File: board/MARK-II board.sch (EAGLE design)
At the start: 168 parts, among them IC1 MAX3243CPWR, IC10 IFX1963TBV, IC11 IFX1963TBV, IC12 ATMEGA48PB-AU, IC13 LD1117S33, IC2 FT230XS, IC3 ENC28J60SS, IC4 PCM5100, IC5 IS42S83200, IC6 MCP7940NSN, IC7 FM24CL16BG, IC8 AT25DN256SS, IC9 10M25SAE144, Q1 25MHz, Q2 32.768kHz, Q3 CMI-1275C-050, Q4 25MHz, Q5 18,432MHz, Q6 22.5792MHz, T1 BC337-16 A1, X1 MINI-USBUX60A-MB-5ST, X10 T821-106A1S100, X11 T821-110A1S100, X12 PJ-002BH-SMT-TR, X13 T821-106A1S100, X2 L717SDE09P1ACH4F, X3 L77HDE15SD1CH4R, X4 MD-60SM, X5 RB1-125BAG1A, X6 SJ1-3535NG, X7 MICROSD-HRS_DM3D, X8 BAT-HLD-002-SMT, X9 T821-120A1S100

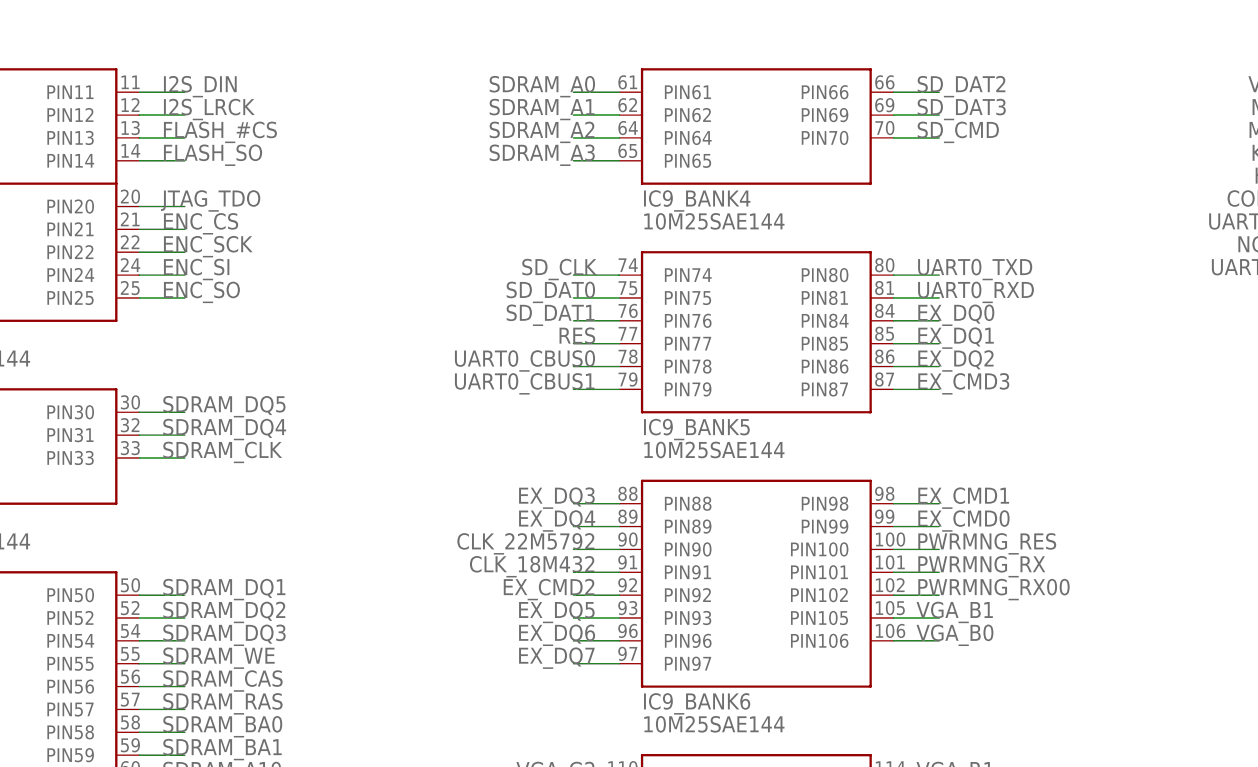
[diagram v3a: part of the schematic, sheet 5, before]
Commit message: Fixed pwrmng uart connection
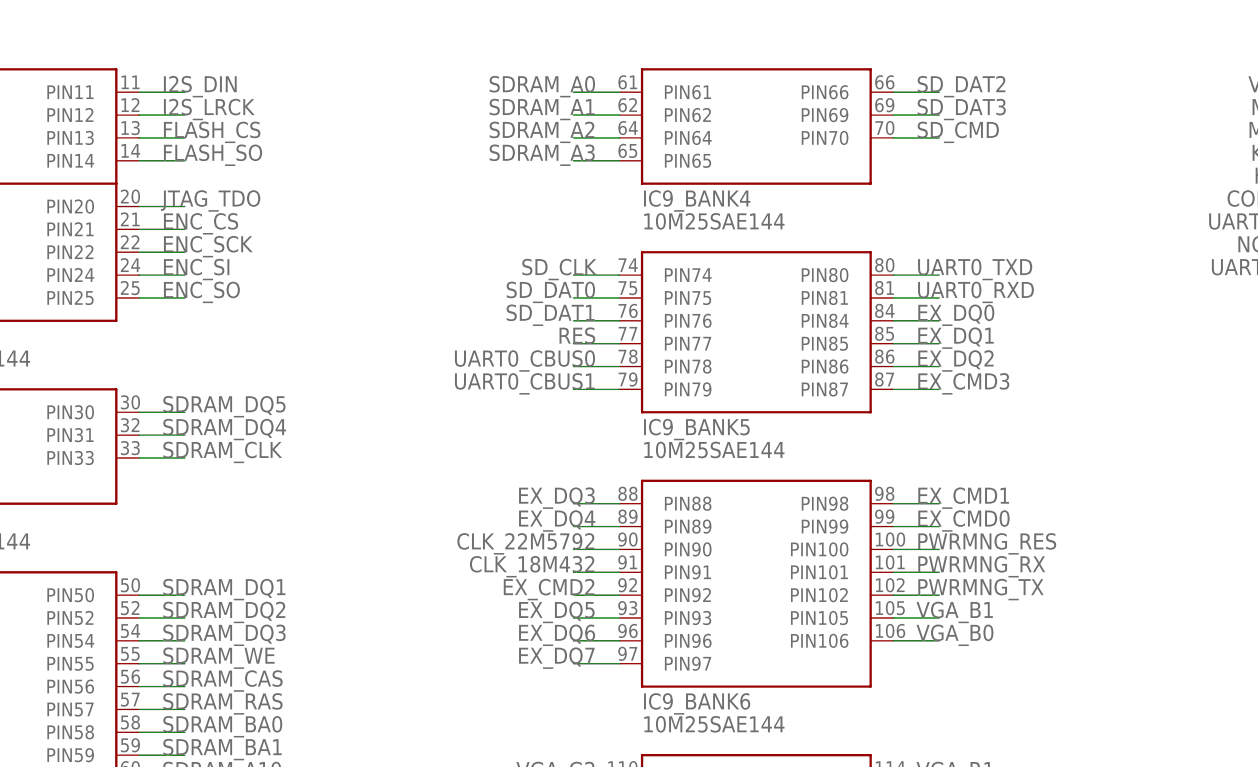
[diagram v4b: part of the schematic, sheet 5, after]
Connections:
- net FLASH_#CS renamed FLASH_CS
- removed net PWRMNG_RX00: IC9_BANK6.PIN102
- net PWRMNG_TX: now also IC9_BANK6.PIN102
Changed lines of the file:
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@@
 </segment>
 </net>
-<net name="FLASH_#CS" class="2">
+<net name="FLASH_CS" class="2">
 <segment>
 <pinref part="IC8" gate="G$1" pin="#CS"/>
@@
 </segment>
 </net>
-<net name="FLASH_#CS" class="2">
+<net name="FLASH_CS" class="2">
 <segment>
 <wire x1="73.66" y1="160.02" x2="68.58" y2="160.02" width="0.1524" layer="91"/>
@@
 </segment>
 </net>
-<net name="PWRMNG_RX00" class="2">
+<net name="PWRMNG_TX" class="2">
 <segment>
 <pinref part="IC9" gate="_BANK6" pin="PIN102"/>

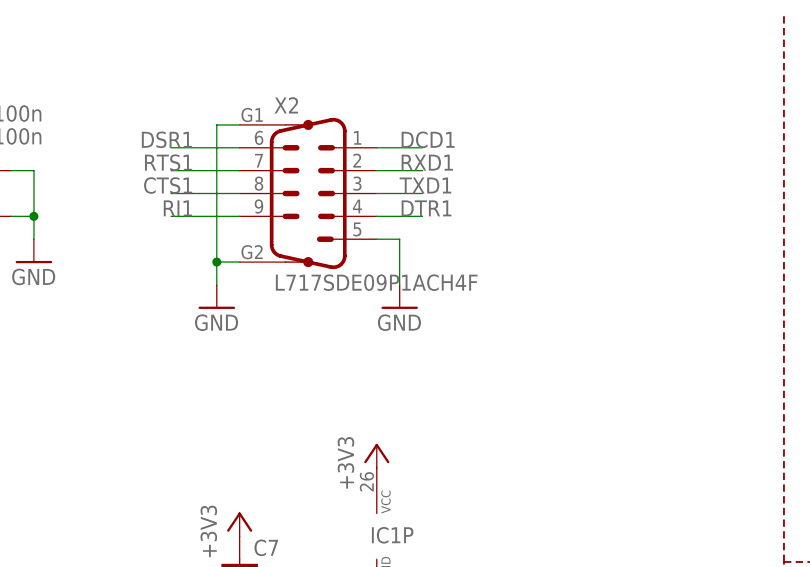
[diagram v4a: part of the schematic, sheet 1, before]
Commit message: Fixed some mistakes on board design
Enc xtal is now on top side
Changed barrel jack holes diameter
Fixed pins pitch on mini DIN con
Changed value of input capacitor
Fixed position of RS232 Dsub con, changed part number
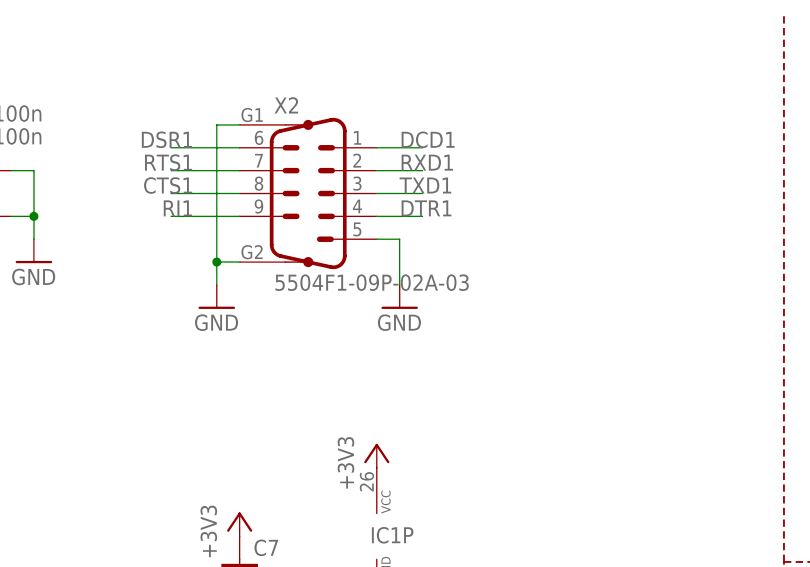
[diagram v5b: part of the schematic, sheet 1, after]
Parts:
- C64: value 1000u -> 470u
- X2: value L717SDE09P1ACH4F -> 5504F1-09P-02A-03; FARNELL 2401240 -> 1848368; MOUSER 523-L717SDE09P1ACH4F -> (none)
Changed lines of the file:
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@@
 <setting verticaltext="up"/>
 </settings>
-<grid distance="0.1" unitdist="inch" unit="inch" style="lines" multiple="1" display="yes" altdistance="0.01" altunitdist="inch" altunit="inch"/>
+<grid distance="0.1" unitdist="inch" unit="inch" style="lines" multiple="1" display="no" altdistance="0.01" altunitdist="inch" altunit="inch"/>
 <layers>
 <layer number="1" name="Top" color="4" fill="1" visible="no" active="no"/>
@@
 <attribute name="MOUSER" value="798-UX60A-MB-5ST"/>
 </part>
-<part name="X2" library="con" deviceset="M09" device="" value="L717SDE09P1ACH4F">
-<attribute name="FARNELL" value="2401240"/>
-<attribute name="MOUSER" value="523-L717SDE09P1ACH4F"/>
+<part name="X2" library="con" deviceset="M09" device="" value="5504F1-09P-02A-03">
+<attribute name="FARNELL" value="1848368"/>
 </part>
 <part name="X3" library="con" deviceset="HF15" device="H" value="L77HDE15SD1CH4R">
@@
 <part name="GND81" library="supply1" library_urn="urn:adsk.eagle:library:371" deviceset="GND" device=""/>
 <part name="GND79" library="supply1" library_urn="urn:adsk.eagle:library:371" deviceset="GND" device=""/>
-<part name="C64" library="misc" deviceset="C-POL" device="E3.5-8" value="1000u">
+<part name="C64" library="misc" deviceset="C-POL" device="E3.5-8" value="470u">
 <attribute name="MOUSER" value="667-EEU-FR1C102L"/>
 </part>
@@
 </instance>
 <instance part="X2" gate="G$1" x="104.14" y="154.94">
-<attribute name="MOUSER" x="104.14" y="154.94" size="1.778" layer="96" display="off"/>
 <attribute name="FARNELL" x="104.14" y="154.94" size="1.778" layer="96" display="off"/>
 </instance>

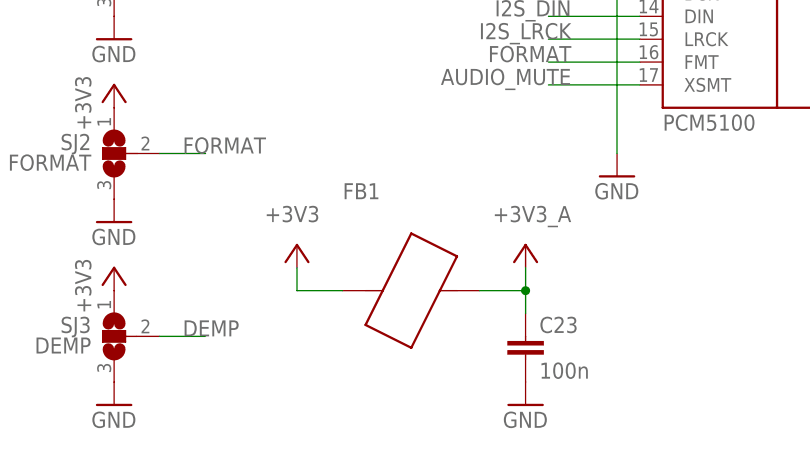
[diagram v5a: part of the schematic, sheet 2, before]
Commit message: Add ferrite beads
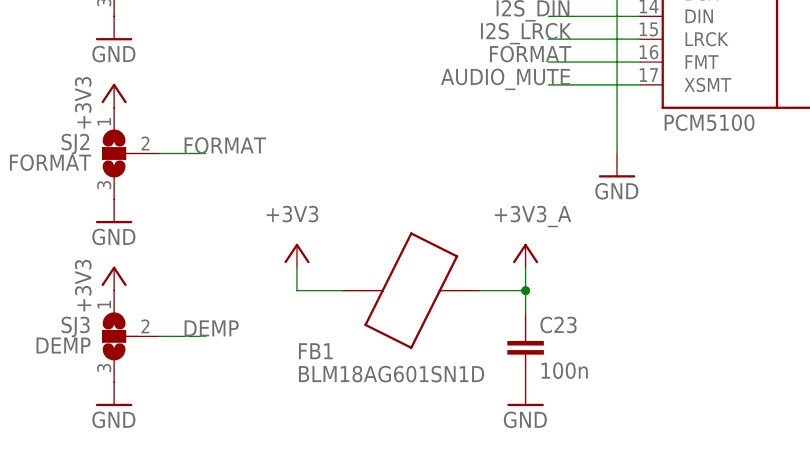
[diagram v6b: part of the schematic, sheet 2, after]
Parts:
- FB1, FB2: value (none) -> BLM18AG601SN1D; MOUSER (none) -> 81-BLM11A601S
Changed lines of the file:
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@@
 <part name="GND26" library="supply1" library_urn="urn:adsk.eagle:library:371" deviceset="GND" device=""/>
 <part name="+3V315" library="supply1" library_urn="urn:adsk.eagle:library:371" deviceset="+3V3" device=""/>
-<part name="FB1" library="misc" deviceset="FERRITE_BEAD" device="603"/>
-<part name="FB2" library="misc" deviceset="FERRITE_BEAD" device="603"/>
+<part name="FB1" library="misc" deviceset="FERRITE_BEAD" device="603" value="BLM18AG601SN1D">
+<attribute name="MOUSER" value="81-BLM11A601S"/>
+</part>
+<part name="FB2" library="misc" deviceset="FERRITE_BEAD" device="603" value="BLM18AG601SN1D">
+<attribute name="MOUSER" value="81-BLM11A601S"/>
+</part>
 <part name="C59" library="misc" deviceset="C" device="C0603" value="100n">
 <attribute name="MOUSER" value="710-885012206046"/>
@@
 <attribute name="VALUE" x="124.46" y="30.48" size="1.778" layer="96" rot="MR0"/>
 </instance>
-<instance part="FB1" gate="G$1" x="134.62" y="22.86"/>
+<instance part="FB1" gate="G$1" x="134.62" y="22.86" smashed="yes">
+<attribute name="NAME" x="121.92" y="15.24" size="1.778" layer="95"/>
+<attribute name="VALUE" x="121.92" y="12.7" size="1.778" layer="96"/>
+<attribute name="MOUSER" x="134.62" y="22.86" size="1.778" layer="96" display="off"/>
+</instance>
 </instances>
 <busses>
@@
 <instance part="+3V341" gate="G$1" x="15.24" y="55.88"/>
 <instance part="GND63" gate="1" x="15.24" y="10.16"/>
-<instance part="FB2" gate="G$1" x="15.24" y="43.18" rot="R270"/>
+<instance part="FB2" gate="G$1" x="15.24" y="43.18" rot="R270">
+<attribute name="MOUSER" x="15.24" y="43.18" size="1.778" layer="96" rot="R270" display="off"/>
+</instance>
 <instance part="C59" gate="G$1" x="233.68" y="43.18">
 <attribute name="MOUSER" x="233.68" y="43.18" size="1.778" layer="96" display="off"/>

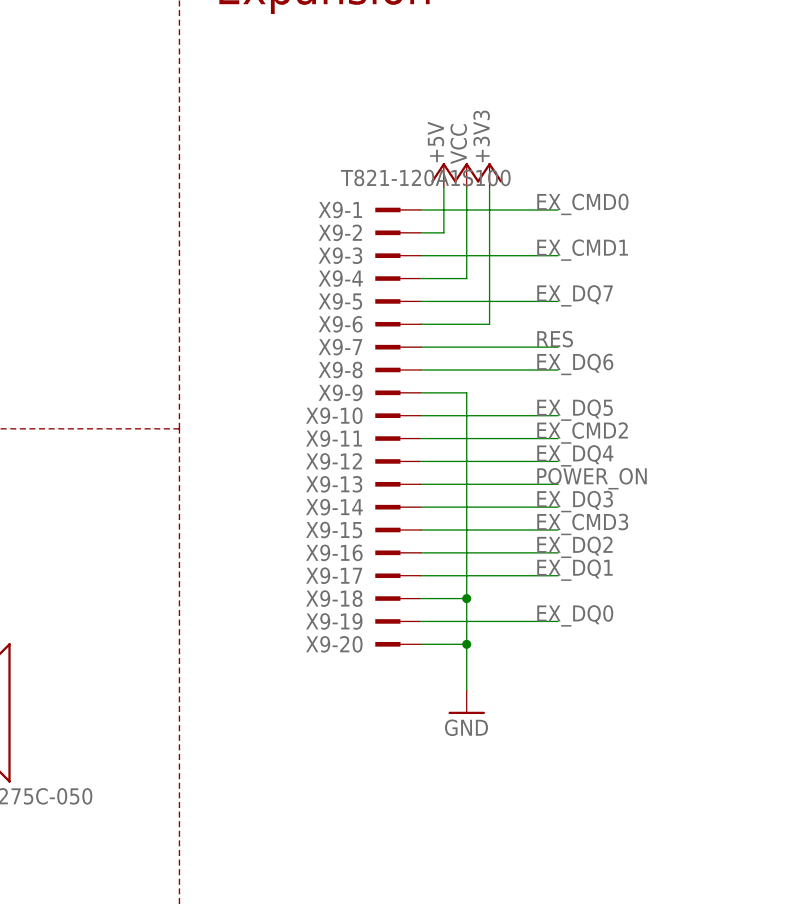
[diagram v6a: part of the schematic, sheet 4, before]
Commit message: Fixed some mistakes in component names
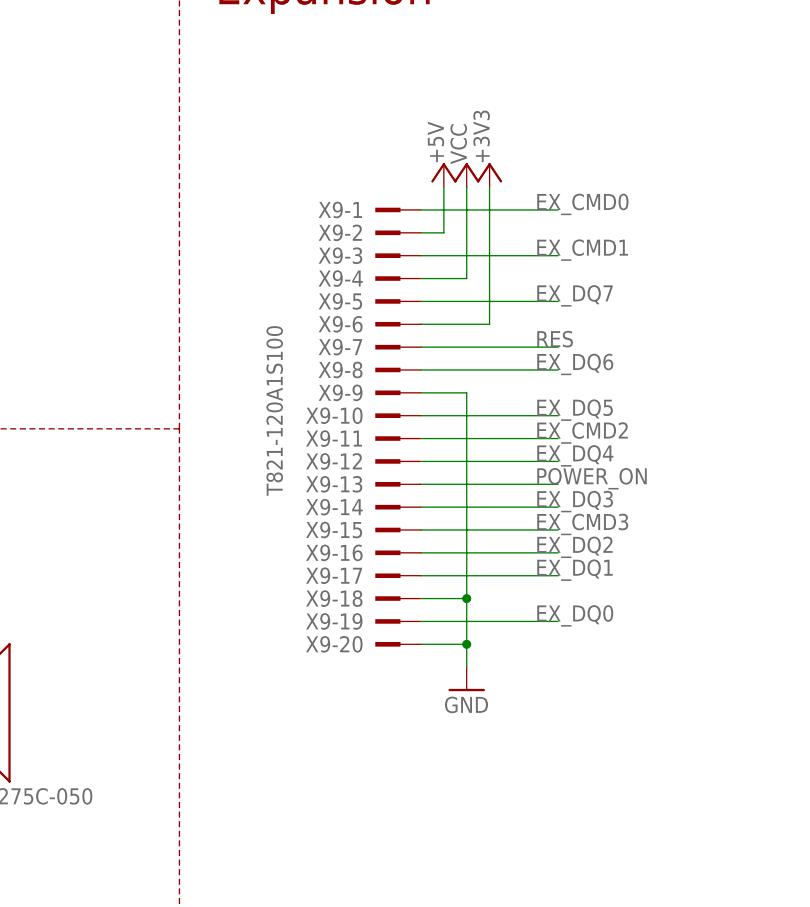
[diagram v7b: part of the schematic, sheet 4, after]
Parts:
- C64: MOUSER 667-EEU-FR1C102L -> 667-EEU-FR1E471Y
- IC5: value IS42S83200 -> AS4C32M8SA
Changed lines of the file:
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@@
 <attribute name="MOUSER" value="989-10M25SAE144C8G"/>
 </part>
-<part name="IC5" library="ic" deviceset="IS42S83200" device="">
+<part name="IC5" library="ic" deviceset="IS42S83200" device="" value="AS4C32M8SA">
 <attribute name="MOUSER" value="913-AS4C32M8SA6TIN"/>
 </part>
@@
 <part name="GND79" library="supply1" library_urn="urn:adsk.eagle:library:371" deviceset="GND" device=""/>
 <part name="C64" library="misc" deviceset="C-POL" device="E3.5-8" value="470u">
-<attribute name="MOUSER" value="667-EEU-FR1C102L"/>
+<attribute name="MOUSER" value="667-EEU-FR1E471Y"/>
 </part>
 <part name="P+10" library="supply1" library_urn="urn:adsk.eagle:library:371" deviceset="VCC" device=""/>
@@
 <attribute name="MOUSER" x="210.82" y="111.76" size="1.778" layer="96" display="off"/>
 </instance>
-<instance part="GND55" gate="1" x="121.92" y="88.9"/>
+<instance part="GND55" gate="1" x="121.92" y="91.44"/>
 <instance part="+3V334" gate="G$1" x="124.46" y="149.86" smashed="yes">
 <attribute name="VALUE" x="124.46" y="149.86" size="1.778" layer="96" rot="R90"/>
@@
 <attribute name="MOUSER" x="121.92" y="20.32" size="1.778" layer="96" rot="MR270" display="off"/>
 </instance>
-<instance part="X9" gate="-1" x="111.76" y="144.78">
+<instance part="X9" gate="-1" x="111.76" y="144.78" smashed="yes">
 <attribute name="FARNELL" x="111.76" y="144.78" size="1.778" layer="96" display="off"/>
+<attribute name="NAME" x="110.49" y="145.669" size="1.778" layer="95" rot="R180"/>
+<attribute name="VALUE" x="101.473" y="113.03" size="1.778" layer="96" rot="R90"/>
 </instance>
 <instance part="X9" gate="-2" x="111.76" y="142.24"/>
@@
 <pinref part="GND55" gate="1" pin="GND"/>
 <wire x1="121.92" y1="101.6" x2="121.92" y2="96.52" width="0.1524" layer="91"/>
-<wire x1="121.92" y1="96.52" x2="121.92" y2="91.44" width="0.1524" layer="91"/>
+<wire x1="121.92" y1="96.52" x2="121.92" y2="93.98" width="0.1524" layer="91"/>
 <wire x1="116.84" y1="96.52" x2="121.92" y2="96.52" width="0.1524" layer="91"/>
 <junction x="121.92" y="96.52"/>
